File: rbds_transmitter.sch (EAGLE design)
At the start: 64 parts, among them IC1 MAX1551, IC2 TPS61030, IC3 MCP4812, IC4 OPA4743UA, Q1 P-Ch, SW1 FSMSM, U3 ATMEGA328, X1 HD44780LCD-1602, Y1 16Mhz

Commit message: didn't really actually work after class
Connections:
- new net OC0A: U3.PD6(AIN0)
- new net OC0B: U3.PD5(T1)
- new net OC1A: U3.PB1(OC1A)
- new net OC1B: U3.PB2(SS/OC1B)
- new net OC2B: U3.PD3(INT1)
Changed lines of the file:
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@@
 <wire x1="251.46" y1="-53.34" x2="251.46" y2="-55.88" width="0.1524" layer="91"/>
 <wire x1="251.46" y1="-55.88" x2="226.06" y2="-55.88" width="0.1524" layer="91"/>
+<label x="228.6" y="-55.88" size="1.778" layer="95"/>
 </segment>
 </net>
@@
 </segment>
 </net>
+<net name="OC2B" class="0">
+<segment>
+<pinref part="U3" gate="G$1" pin="PD3(INT1)"/>
+<wire x1="83.82" y1="40.64" x2="93.98" y2="40.64" width="0.1524" layer="91"/>
+<label x="86.36" y="40.64" size="1.778" layer="95"/>
+</segment>
+</net>
+<net name="OC0B" class="0">
+<segment>
+<pinref part="U3" gate="G$1" pin="PD5(T1)"/>
+<wire x1="83.82" y1="35.56" x2="93.98" y2="35.56" width="0.1524" layer="91"/>
+<label x="86.36" y="35.56" size="1.778" layer="95"/>
+</segment>
+</net>
+<net name="OC0A" class="0">
+<segment>
+<pinref part="U3" gate="G$1" pin="PD6(AIN0)"/>
+<wire x1="83.82" y1="33.02" x2="93.98" y2="33.02" width="0.1524" layer="91"/>
+<label x="86.36" y="33.02" size="1.778" layer="95"/>
+</segment>
+</net>
+<net name="OC1A" class="0">
+<segment>
+<pinref part="U3" gate="G$1" pin="PB1(OC1A)"/>
+<wire x1="83.82" y1="22.86" x2="93.98" y2="22.86" width="0.1524" layer="91"/>
+<label x="86.36" y="22.86" size="1.778" layer="95"/>
+</segment>
+</net>
+<net name="OC1B" class="0">
+<segment>
+<pinref part="U3" gate="G$1" pin="PB2(SS/OC1B)"/>
+<wire x1="83.82" y1="20.32" x2="93.98" y2="20.32" width="0.1524" layer="91"/>
+<label x="86.36" y="20.32" size="1.778" layer="95"/>
+</segment>
+</net>

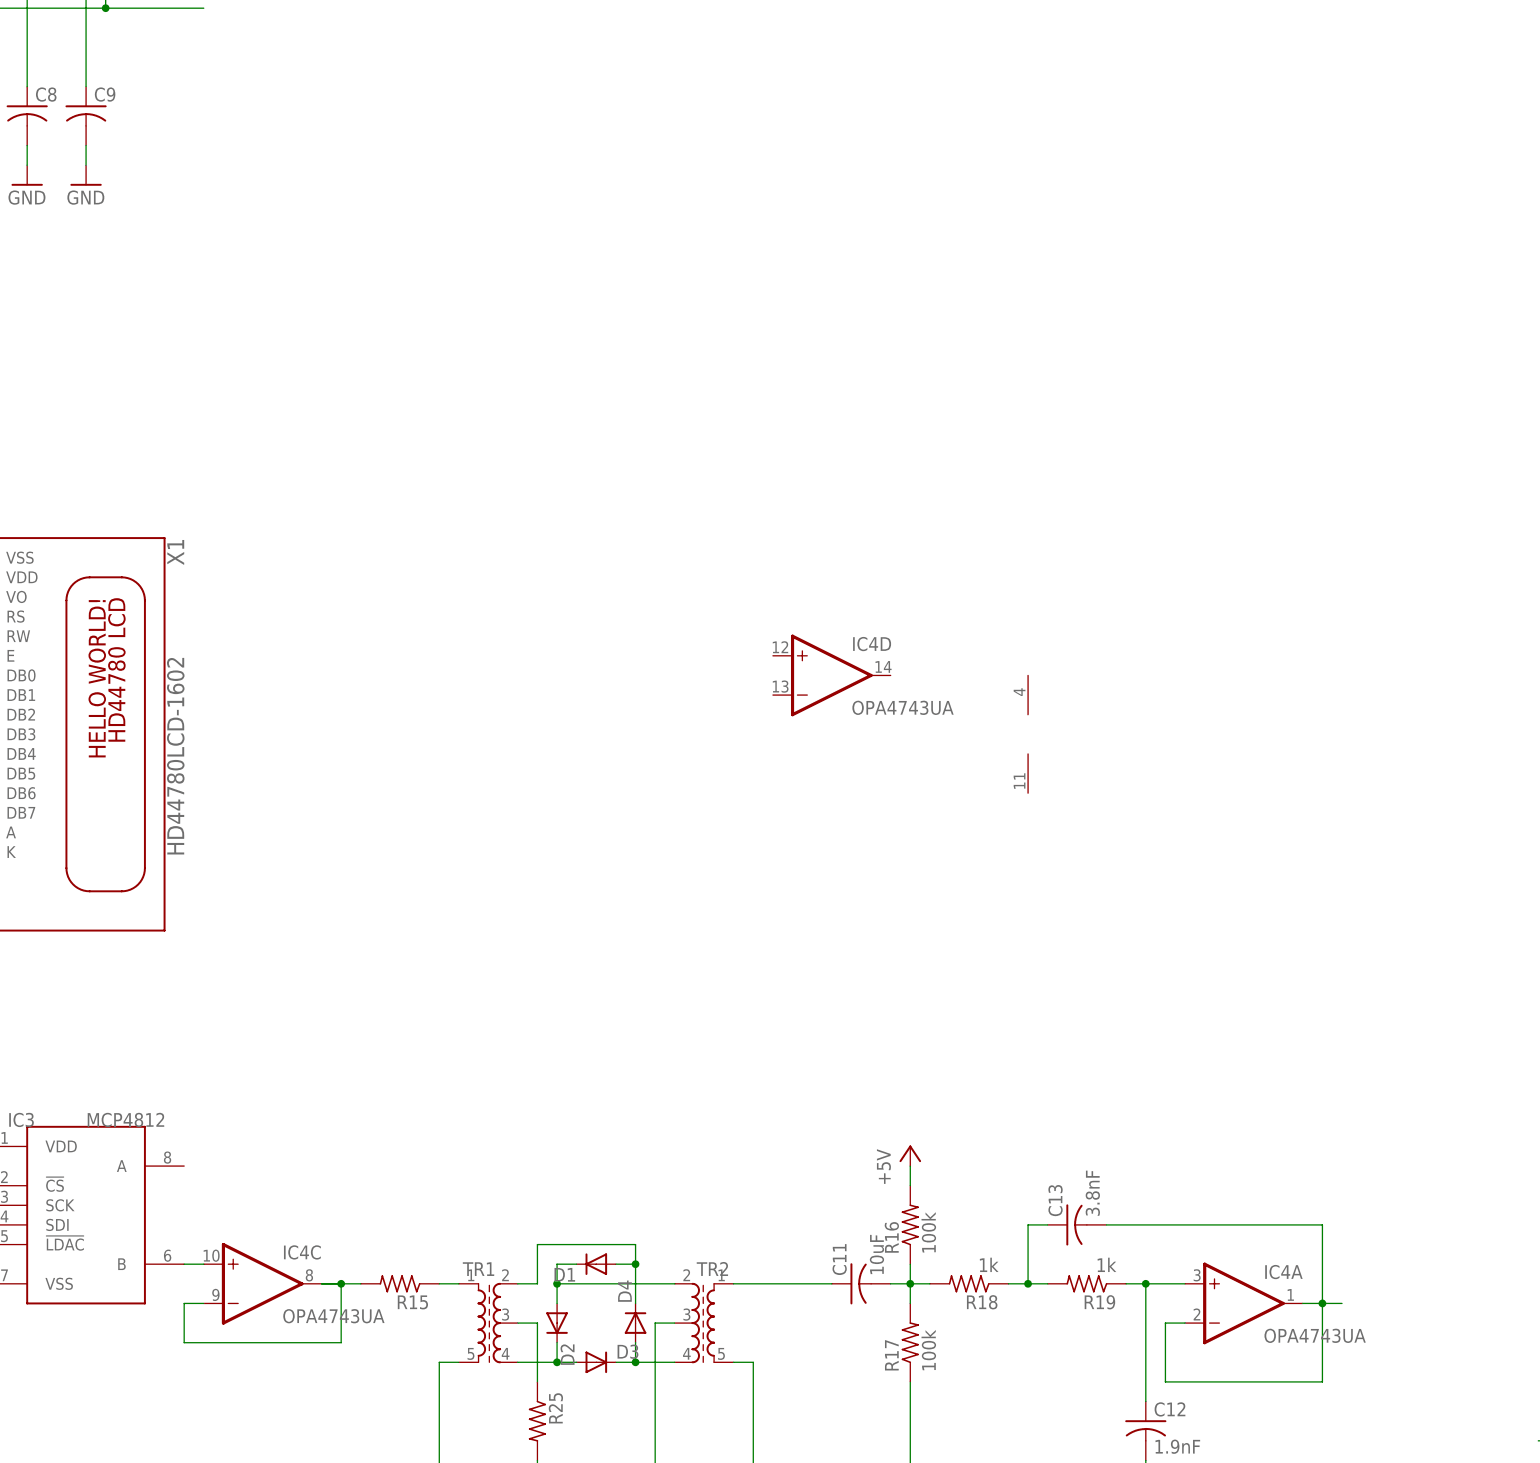
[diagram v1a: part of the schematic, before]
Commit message: adding filters for pilot/sound
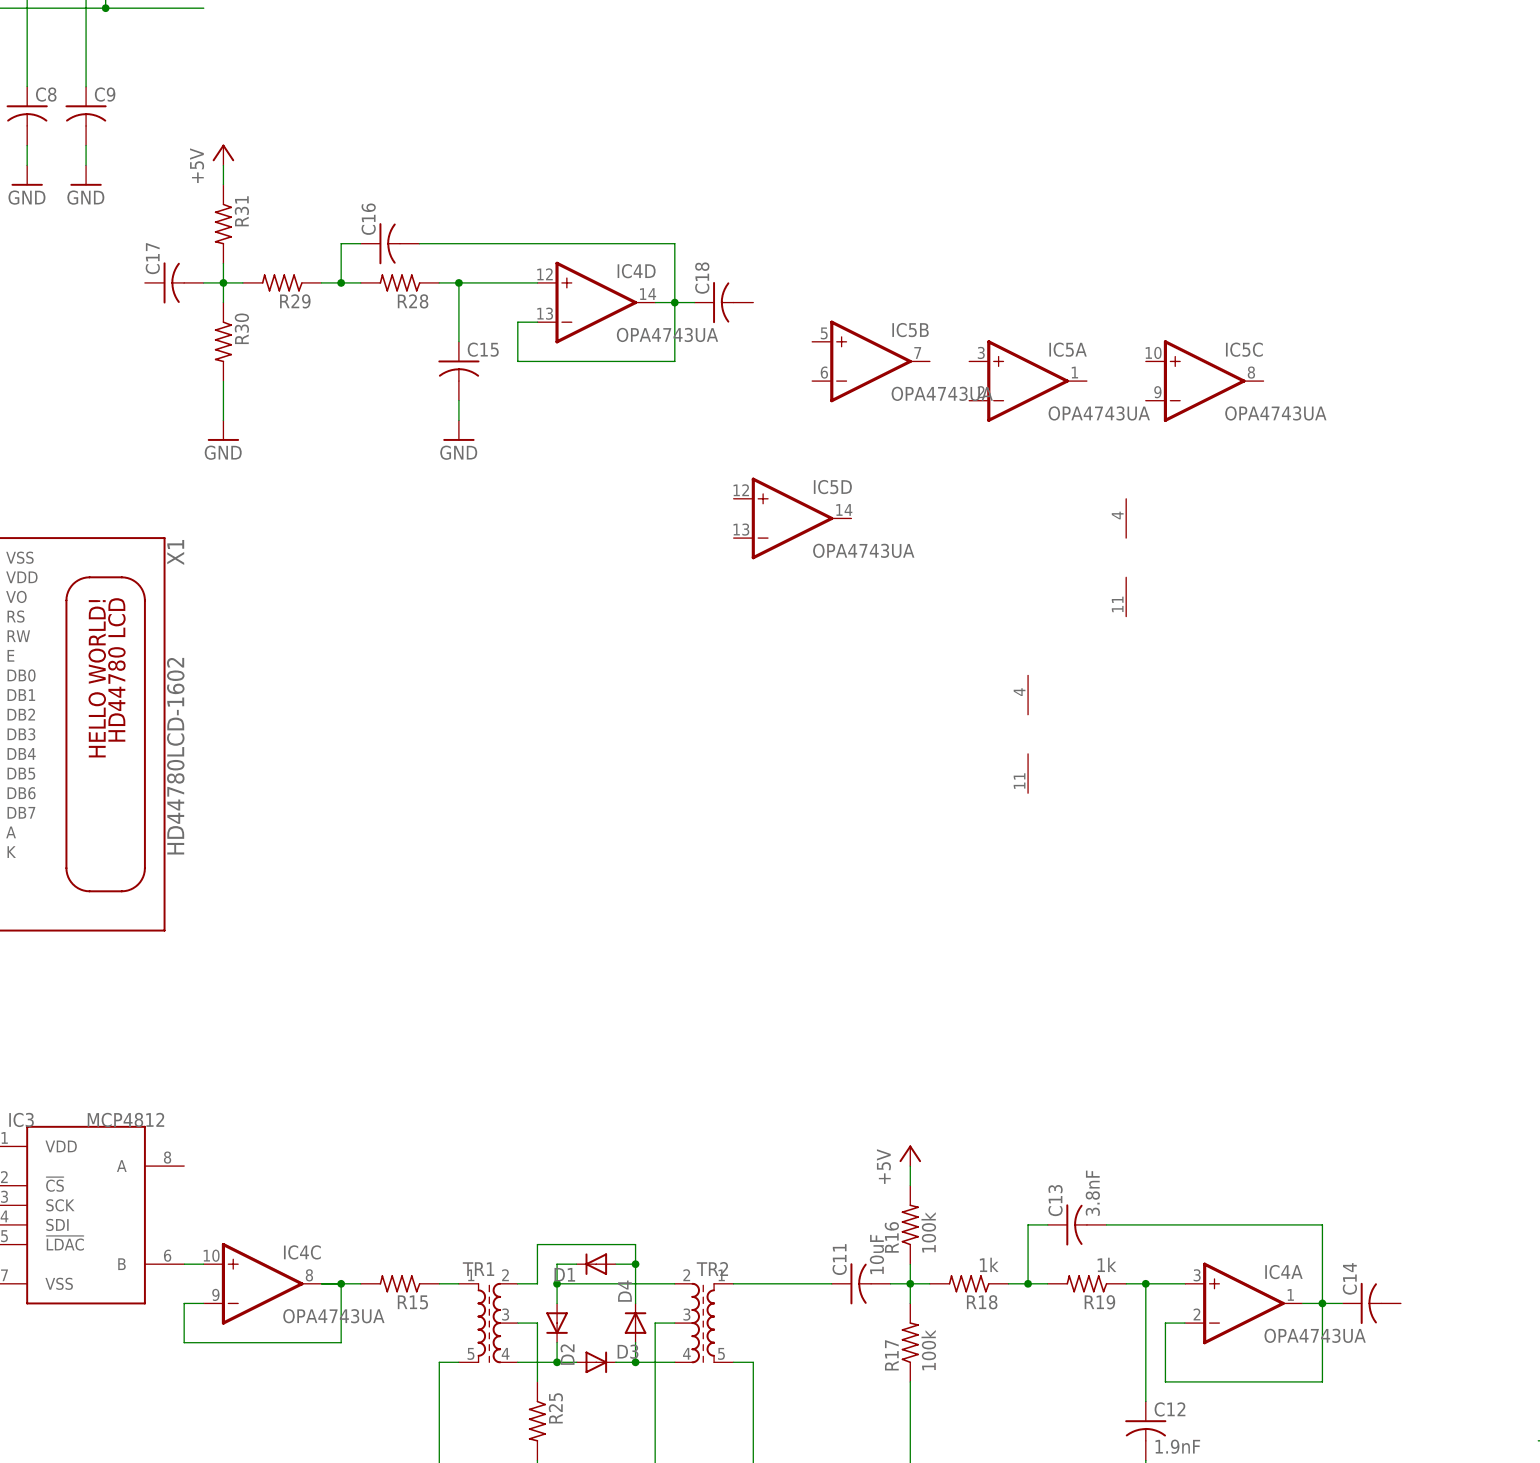
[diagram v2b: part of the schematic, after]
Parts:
- added C14, C15, C16, C17, C18: (no value), adafruit:C-USC1206
- added IC5: OPA4743UA, linear:OPA4743UA
- added R28, R29, R30, R31: (no value), adafruit:R-US_R1206
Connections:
- new net N$34: C15.1, IC4D.+IN, R28.1
- new net N$35: C16.2, C18.1, IC4D.-IN, IC4D.OUT
- new net N$36: C16.1, R28.2, R29.1
- new net N$38: C17.2, R29.2, R30.1, R31.2
- net +5V: now also R31.1
- net GND: now also C15.2, R30.2
- net N$24: now also C14.1
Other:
- moved on the sheet: IC4D
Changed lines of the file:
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@@
 <part name="GND29" library="sparkfun" deviceset="GND" device=""/>
 <part name="GND30" library="sparkfun" deviceset="GND" device=""/>
+<part name="IC5" library="linear" deviceset="OPA4743" device="UA"/>
+<part name="C14" library="adafruit" deviceset="C-US" device="C1206"/>
+<part name="C15" library="adafruit" deviceset="C-US" device="C1206"/>
+<part name="C16" library="adafruit" deviceset="C-US" device="C1206"/>
+<part name="C17" library="adafruit" deviceset="C-US" device="C1206"/>
+<part name="C18" library="adafruit" deviceset="C-US" device="C1206"/>
+<part name="R28" library="adafruit" deviceset="R-US_" device="R1206"/>
+<part name="R29" library="adafruit" deviceset="R-US_" device="R1206"/>
+<part name="R30" library="adafruit" deviceset="R-US_" device="R1206"/>
+<part name="R31" library="adafruit" deviceset="R-US_" device="R1206"/>
+<part name="GND31" library="sparkfun" deviceset="GND" device=""/>
+<part name="GND32" library="sparkfun" deviceset="GND" device=""/>
+<part name="P+10" library="supply1" deviceset="+5V" device=""/>
 </parts>
 <sheets>
@@
 <instance part="IC4" gate="B" x="419.1" y="-30.48"/>
 <instance part="IC4" gate="C" x="215.9" y="-30.48"/>
-<instance part="IC4" gate="D" x="289.56" y="48.26"/>
+<instance part="IC4" gate="D" x="259.08" y="96.52"/>
 <instance part="IC4" gate="P" x="314.96" y="40.64"/>
 <instance part="R16" gate="G$1" x="299.72" y="-22.86" rot="R90"/>
@@
 <instance part="GND29" gate="1" x="383.54" y="-91.44"/>
 <instance part="GND30" gate="1" x="383.54" y="-68.58"/>
+<instance part="IC5" gate="D" x="284.48" y="68.58"/>
+<instance part="IC5" gate="A" x="314.96" y="86.36"/>
+<instance part="IC5" gate="B" x="294.64" y="88.9"/>
+<instance part="IC5" gate="C" x="337.82" y="86.36"/>
+<instance part="IC5" gate="P" x="327.66" y="63.5"/>
+<instance part="C14" gate="G$1" x="358.14" y="-33.02" rot="R90"/>
+<instance part="C15" gate="G$1" x="241.3" y="88.9"/>
+<instance part="C16" gate="G$1" x="231.14" y="104.14" rot="R90"/>
+<instance part="C17" gate="G$1" x="203.2" y="99.06" rot="R90"/>
+<instance part="C18" gate="G$1" x="274.32" y="96.52" rot="R90"/>
+<instance part="R28" gate="G$1" x="233.68" y="99.06" rot="R180"/>
+<instance part="R29" gate="G$1" x="218.44" y="99.06" rot="R180"/>
+<instance part="R30" gate="G$1" x="210.82" y="91.44" rot="R270"/>
+<instance part="R31" gate="G$1" x="210.82" y="106.68" rot="R270"/>
+<instance part="GND31" gate="1" x="210.82" y="78.74"/>
+<instance part="GND32" gate="1" x="241.3" y="78.74"/>
+<instance part="P+10" gate="1" x="210.82" y="116.84"/>
 </instances>
 <busses>
@@
 <pinref part="R27" gate="G$1" pin="A"/>
 <wire x1="383.54" y1="-86.36" x2="383.54" y2="-88.9" width="0.1524" layer="91"/>
+</segment>
+<segment>
+<pinref part="C15" gate="G$1" pin="2"/>
+<pinref part="GND32" gate="1" pin="GND"/>
+<wire x1="241.3" y1="81.28" x2="241.3" y2="83.82" width="0.1524" layer="91"/>
+</segment>
+<segment>
+<pinref part="R30" gate="G$1" pin="2"/>
+<pinref part="GND31" gate="1" pin="GND"/>
+<wire x1="210.82" y1="81.28" x2="210.82" y2="86.36" width="0.1524" layer="91"/>
 </segment>
 </net>
@@
 <wire x1="299.72" y1="-15.24" x2="299.72" y2="-17.78" width="0.1524" layer="91"/>
 </segment>
+<segment>
+<pinref part="R31" gate="G$1" pin="1"/>
+<pinref part="P+10" gate="1" pin="+5V"/>
+<wire x1="210.82" y1="114.3" x2="210.82" y2="111.76" width="0.1524" layer="91"/>
+</segment>
 </net>
 <net name="ISP-MISO" class="0">
@@
 <wire x1="325.12" y1="-22.86" x2="353.06" y2="-22.86" width="0.1524" layer="91"/>
 <wire x1="353.06" y1="-22.86" x2="353.06" y2="-33.02" width="0.1524" layer="91"/>
+<pinref part="C14" gate="G$1" pin="1"/>
 </segment>
 </net>
@@
 </segment>
 </net>
+<net name="N$34" class="0">
+<segment>
+<pinref part="IC4" gate="D" pin="+IN"/>
+<pinref part="R28" gate="G$1" pin="1"/>
+<wire x1="238.76" y1="99.06" x2="241.3" y2="99.06" width="0.1524" layer="91"/>
+<pinref part="C15" gate="G$1" pin="1"/>
+<wire x1="241.3" y1="99.06" x2="251.46" y2="99.06" width="0.1524" layer="91"/>
+<wire x1="241.3" y1="91.44" x2="241.3" y2="99.06" width="0.1524" layer="91"/>
+<junction x="241.3" y="99.06"/>
+</segment>
+</net>
+<net name="N$35" class="0">
+<segment>
+<pinref part="IC4" gate="D" pin="-IN"/>
+<wire x1="251.46" y1="93.98" x2="248.92" y2="93.98" width="0.1524" layer="91"/>
+<wire x1="248.92" y1="93.98" x2="248.92" y2="88.9" width="0.1524" layer="91"/>
+<wire x1="248.92" y1="88.9" x2="269.24" y2="88.9" width="0.1524" layer="91"/>
+<wire x1="269.24" y1="88.9" x2="269.24" y2="96.52" width="0.1524" layer="91"/>
+<pinref part="IC4" gate="D" pin="OUT"/>
+<wire x1="269.24" y1="96.52" x2="266.7" y2="96.52" width="0.1524" layer="91"/>
+<pinref part="C16" gate="G$1" pin="2"/>
+<wire x1="236.22" y1="104.14" x2="269.24" y2="104.14" width="0.1524" layer="91"/>
+<wire x1="269.24" y1="104.14" x2="269.24" y2="96.52" width="0.1524" layer="91"/>
+<junction x="269.24" y="96.52"/>
+<pinref part="C18" gate="G$1" pin="1"/>
+<wire x1="271.78" y1="96.52" x2="269.24" y2="96.52" width="0.1524" layer="91"/>
+</segment>
+</net>
+<net name="N$36" class="0">
+<segment>
+<pinref part="R28" gate="G$1" pin="2"/>
+<wire x1="228.6" y1="99.06" x2="226.06" y2="99.06" width="0.1524" layer="91"/>
+<wire x1="226.06" y1="99.06" x2="226.06" y2="104.14" width="0.1524" layer="91"/>
+<pinref part="C16" gate="G$1" pin="1"/>
+<wire x1="226.06" y1="104.14" x2="228.6" y2="104.14" width="0.1524" layer="91"/>
+<junction x="226.06" y="99.06"/>
+<pinref part="R29" gate="G$1" pin="1"/>
+<wire x1="223.52" y1="99.06" x2="226.06" y2="99.06" width="0.1524" layer="91"/>
+</segment>
+</net>
+<net name="N$38" class="0">
+<segment>
+<pinref part="R30" gate="G$1" pin="1"/>
+<pinref part="R31" gate="G$1" pin="2"/>
+<wire x1="210.82" y1="96.52" x2="210.82" y2="99.06" width="0.1524" layer="91"/>
+<pinref part="R29" gate="G$1" pin="2"/>
+<wire x1="210.82" y1="99.06" x2="210.82" y2="101.6" width="0.1524" layer="91"/>
+<wire x1="213.36" y1="99.06" x2="210.82" y2="99.06" width="0.1524" layer="91"/>
+<pinref part="C17" gate="G$1" pin="2"/>
+<wire x1="208.28" y1="99.06" x2="210.82" y2="99.06" width="0.1524" layer="91"/>
+<junction x="210.82" y="99.06"/>
+</segment>
+</net>
